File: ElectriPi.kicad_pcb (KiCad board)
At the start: 2 copper layers, 65 x 56 mm, 37 parts, among them J1 2444, J3 JST XH 01x02, J6 Raspberry_Pi_2_3, J8 JST XH 01x02, Q1 30V 4A 44mΩ, Q2 50nA 150V 200mW 200mA, Q3 30V 4A 44mΩ, U1 XL4015

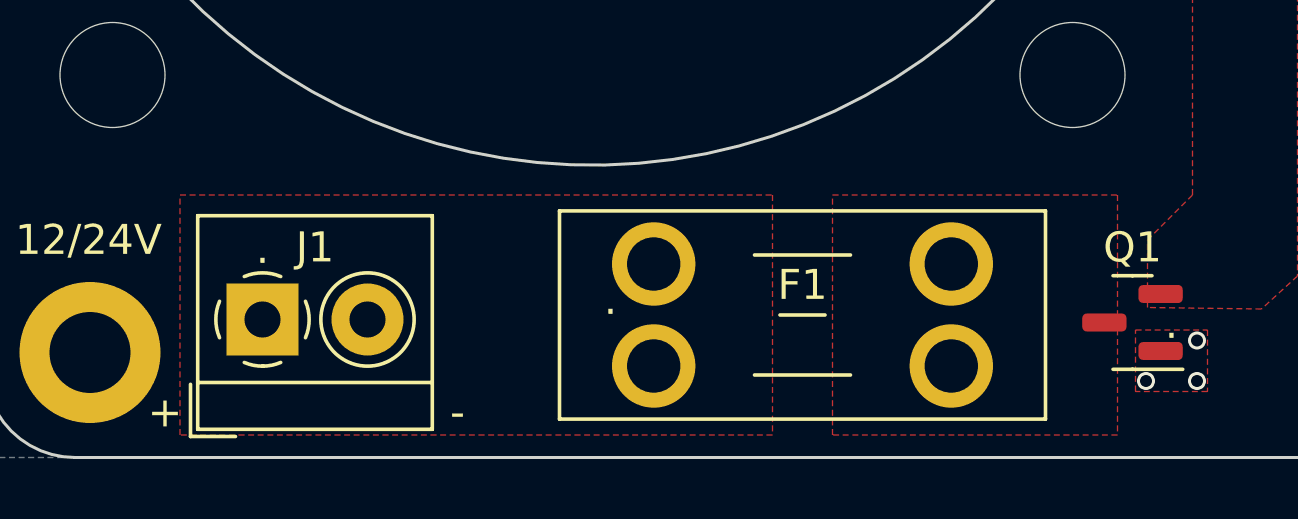
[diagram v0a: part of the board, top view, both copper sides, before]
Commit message: Bladefuse holder switched to Littelfuse nano 2 fuse holder
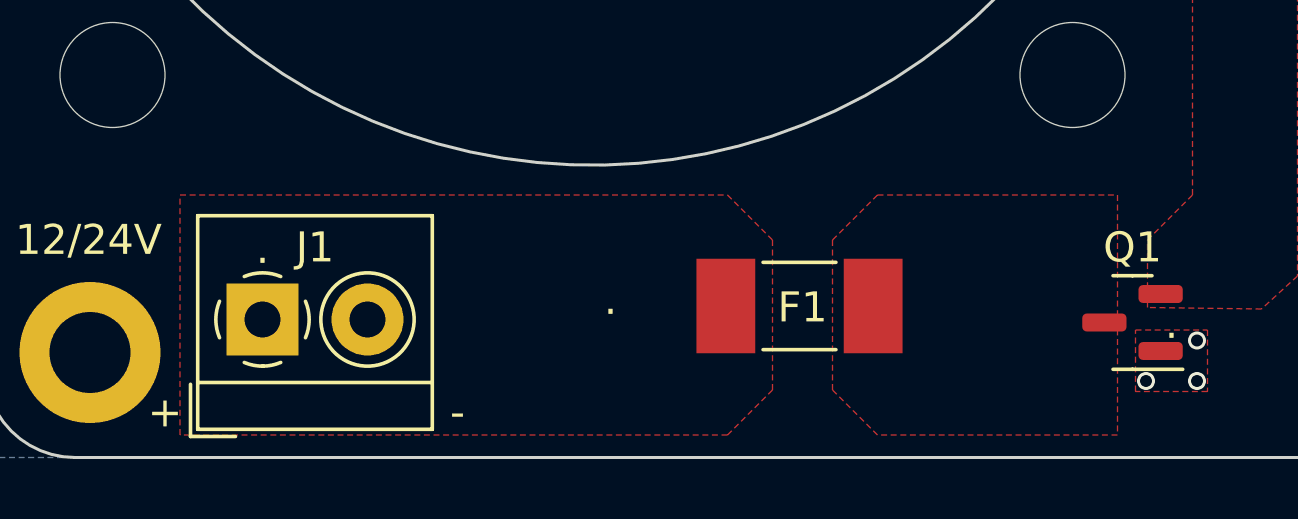
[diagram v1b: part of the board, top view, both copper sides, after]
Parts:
- F1: footprint Fuse:Fuseholder_Blade_Mini_Keystone_3568 -> Fuse:Fuse_Littelfuse-NANO2-451_453
- moved F1 5.06 mm to (112.4, 104.2)

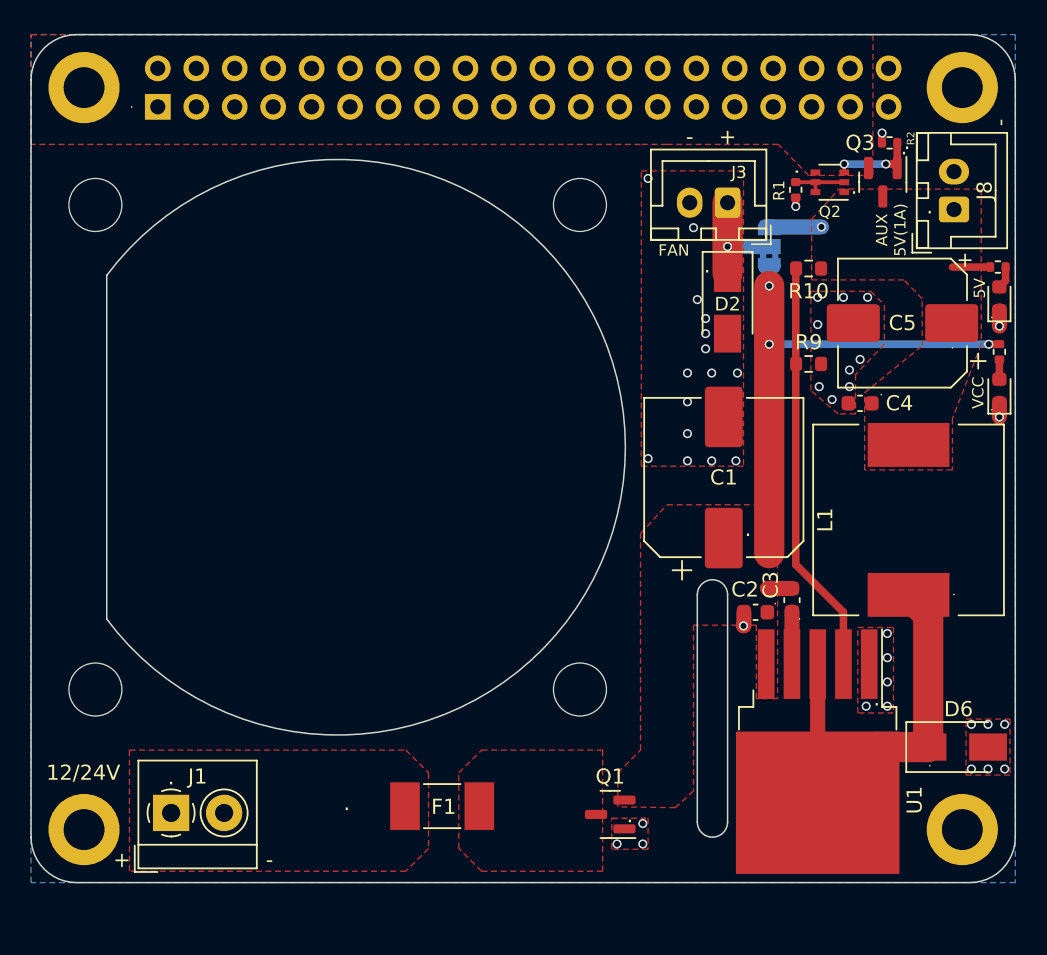
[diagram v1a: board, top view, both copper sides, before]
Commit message: F.Silk, Fan passthough, Fuse, XH input and designator changes
- Added more pin notes to 40Pin GPIO
- Added cutout to fan hole to allow passthrough from reverse mounting
- customised F1 Littelfuse footprint to correctly suit NANO 2 footprint
- Add JST XH Input Option
- Moved superfluous reference designators to hidden layer (user2)
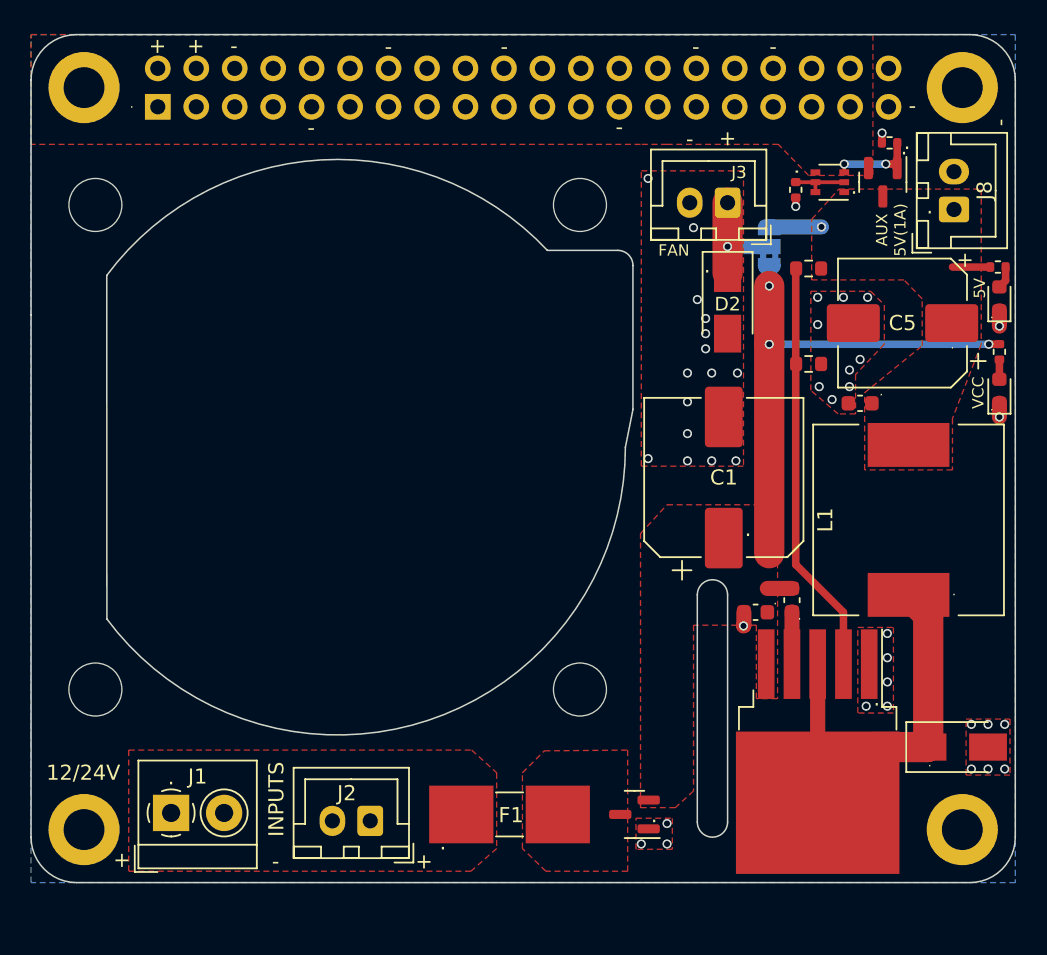
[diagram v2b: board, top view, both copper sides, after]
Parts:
- added J2: JST XH 01x02, Connector_JST:JST_XH_B2B-XH-A_1x02_P2.50mm_Vertical, F.Cu at (107.7, 105.2)
- moved F1 4.48 mm to (116.8, 104.8)
- moved Q1 1.60 mm to (125.1, 104.8)
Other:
- outline, holes or cut-outs redrawn
- board text added: "INPUTS"

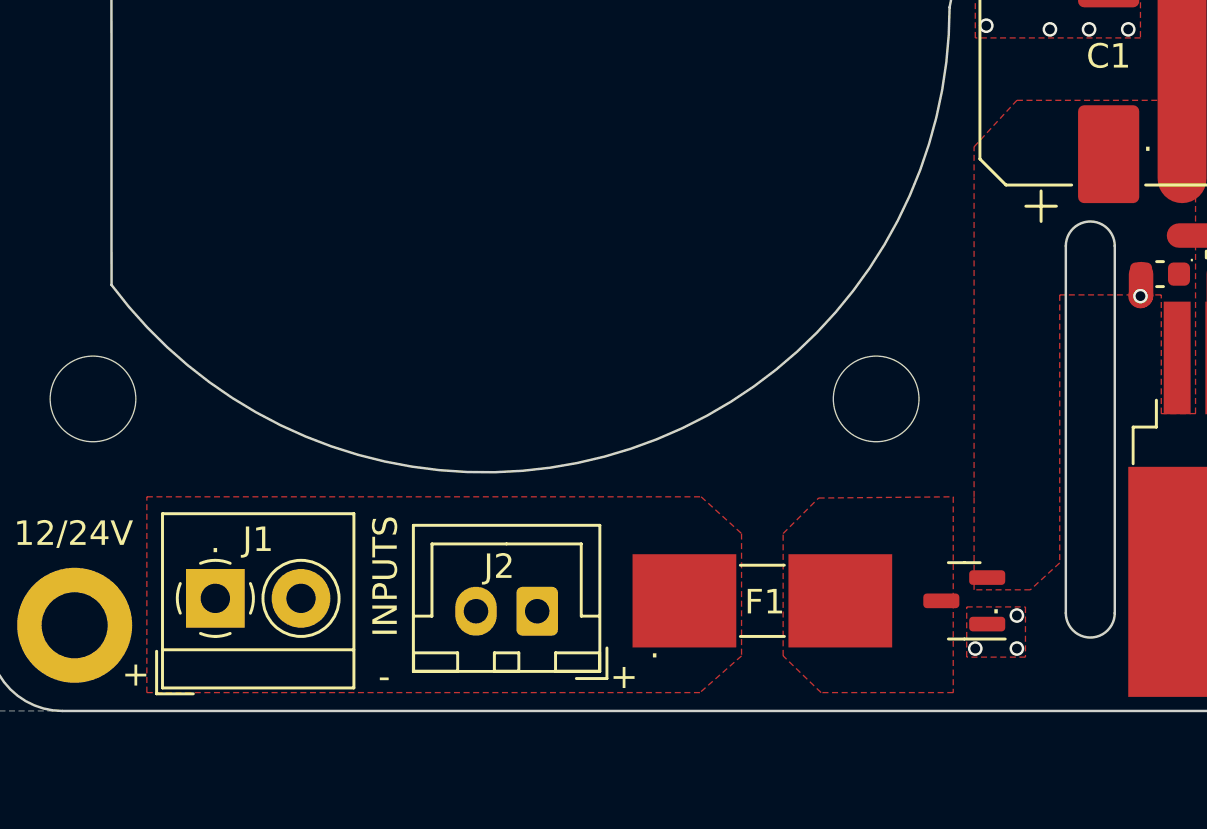
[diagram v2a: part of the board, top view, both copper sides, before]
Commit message: Adding ICL footprint and schematic symbol
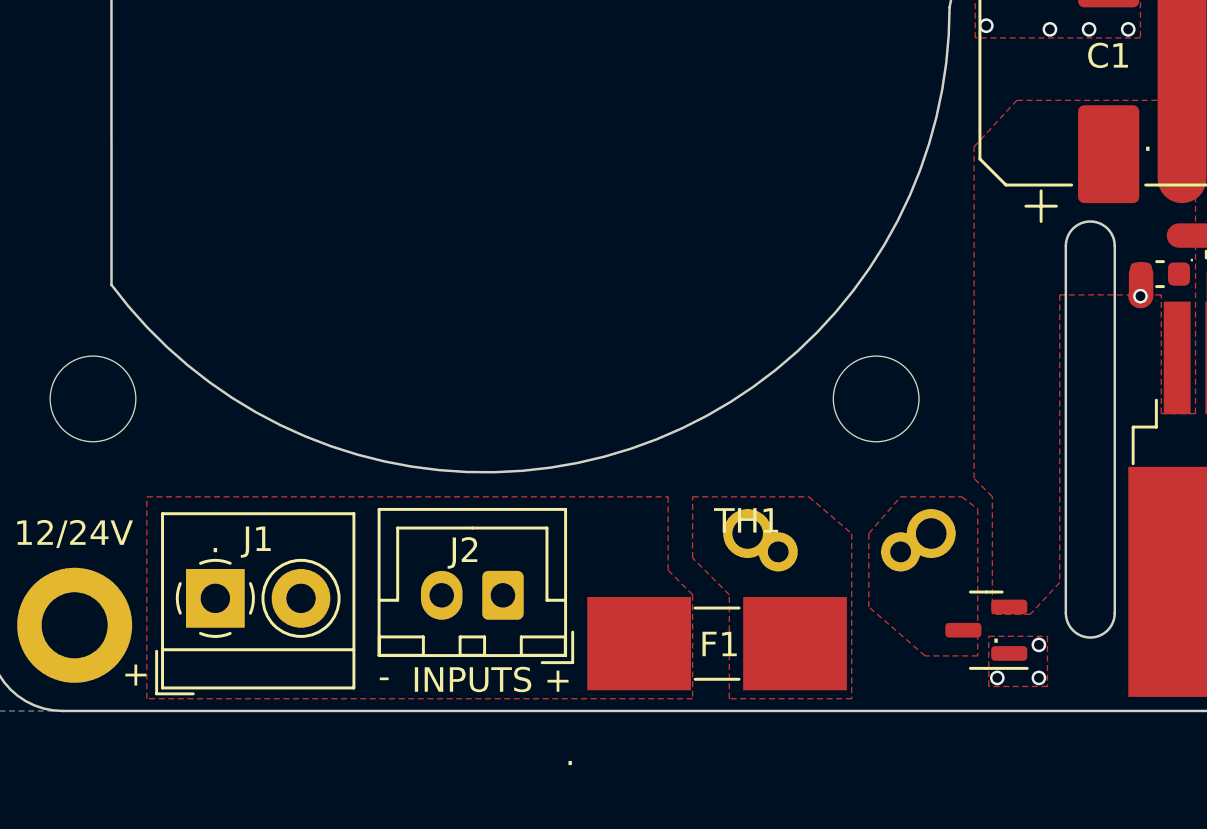
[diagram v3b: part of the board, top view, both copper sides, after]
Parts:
- added TH1: ICL, Inrush_Limiter:5_OR_7pt5_PITCH_ICL, F.Cu at (116.2, 102.0)
- moved F1 2.55 mm to (115.0, 106.5)
- moved J2 1.54 mm to (106.2, 104.5)
- moved Q1 1.50 mm to (126.0, 106.0)
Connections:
- Q1 pad 3: Net-(F1-Pad2) -> Net-(Q1-Pad3)
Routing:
- added copper zone on F.Cu, net Net-(Q1-Pad3)
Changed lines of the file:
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@@
   (net 43 "unconnected-(J6-Pad23)")
   (net 44 "unconnected-(J6-Pad24)")
+  (net 45 "Net-(Q1-Pad3)")
   (footprint "Connector_JST:JST_XH_B2B-XH-A_1x02_P2.50mm_Vertical" (layer "F.Cu")
     (at 146.2 64.8 90)
@@
   )
   (footprint "Connector_JST:JST_XH_B2B-XH-A_1x02_P2.50mm_Vertical" (layer "F.Cu")
-    (at 107.65 105.175 180)
+    (at 106.25 104.525 180)
     (descr "JST XH series connector, B2B-XH-A (http://www.jst-mfg.com/product/pdf/eng/eXH.pdf), generated with kicad-footprint-generator")
     (tags "connector JST XH vertical")
@@
   )
   (footprint "Package_TO_SOT_SMD:SOT-23" (layer "F.Cu")
-    (at 125.1 104.75 180)
+    (at 126 105.95 180)
     (descr "SOT, 3 Pin (https://www.jedec.org/system/files/docs/to-236h.pdf variant AB), generated with kicad-footprint-generator ipc_gullwing_generator.py")
     (tags "SOT TO_SOT_SMD")
@@
       (net 1 "VCC") (pinfunction "S") (pintype "passive"))
     (pad "3" smd roundrect (at 0.9375 0 180) (size 1.475 0.6) (layers "F.Cu" "F.Paste" "F.Mask") (roundrect_rratio 0.25)
-      (net 9 "Net-(F1-Pad2)") (pinfunction "D") (pintype "passive"))
+      (net 45 "Net-(Q1-Pad3)") (pinfunction "D") (pintype "passive"))
     (model "${KICAD6_3DMODEL_DIR}/Package_TO_SOT_SMD.3dshapes/SOT-23.wrl"
       (offset (xyz 0 0 0))
@@
   )
   (footprint "Fuse:Fuse_Littelfuse-NANO2-451_453" (layer "F.Cu")
-    (at 116.85 104.75)
+    (at 115 106.5)
     (descr "Littelfuse NANO2 https://www.littelfuse.com/~/media/electronics/datasheets/fuses/littelfuse_fuse_451_453_datasheet.pdf.pdf")
     (tags "Fuse Nano2")
@@
     )
   )
+  (footprint "Inrush_Limiter:5_OR_7pt5_PITCH_ICL" (layer "F.Cu")
+    (at 116.25 102)
+    (property "Sheetfile" "ElectriPi.kicad_sch")
+    (property "Sheetname" "")
+    (attr through_hole)
+    (fp_text reference "TH1" (at 0 -0.5 unlocked) (layer "F.SilkS")
+      (effects (font (size 1 1) (thickness 0.15)))
+    )
+    (fp_text value "ICL" (at 0 1 unlocked) (layer "F.Fab")
+      (effects (font (size 1 1) (thickness 0.15)))
+    )
+    (pad "1" thru_hole circle (at 1.25 0.75) (size 1.6 1.6) (drill 0.85) (layers *.Cu *.Mask)
+      (net 9 "Net-(F1-Pad2)") (pintype "passive"))
+    (pad "1" thru_hole circle (at 0 0) (size 2 2) (drill 1.25) (layers *.Cu *.Mask)
+      (net 9 "Net-(F1-Pad2)") (pintype "passive"))
+    (pad "2" thru_hole circle (at 7.5 0) (size 2 2) (drill 1.25) (layers *.Cu *.Mask)
+      (net 45 "Net-(Q1-Pad3)") (pintype "passive"))
+    (pad "2" thru_hole circle (at 6.25 0.75) (size 1.6 1.6) (drill 0.85) (layers *.Cu *.Mask)
+      (net 45 "Net-(Q1-Pad3)") (pintype "passive"))
+  )
   (footprint "Resistor_SMD:R_0402_1005Metric" (layer "F.Cu")
     (at 149.2 74.2 90)
@@
     (effects (font (size 1 1) (thickness 0.15)))
   )
-  (gr_text "INPUTS" (at 101.45 103.75 90) (layer "F.SilkS")
+  (gr_text "INPUTS" (at 105 108) (layer "F.SilkS")
     (effects (font (size 1 1) (thickness 0.15)))
   )
-  (gr_text "." (at 126.4 104.8) (layer "F.SilkS")
+  (gr_text "." (at 126.4 106) (layer "F.SilkS")
     (effects (font (size 1 1) (thickness 0.15)))
   )
@@
     (effects (font (size 1 1) (thickness 0.153)))
   )
-  (gr_text "+" (at 111.2 107.85) (layer "F.SilkS")
+  (gr_text "+" (at 108.5 108) (layer "F.SilkS")
     (effects (font (size 1 1) (thickness 0.15)))
   )
@@
     (effects (font (size 1 1) (thickness 0.153)))
   )
-  (gr_text "." (at 112.45 106.6) (layer "F.SilkS")
+  (gr_text "." (at 109 111) (layer "F.SilkS")
     (effects (font (size 1 1) (thickness 0.15)))
   )
@@
   (via (at 149.2 78.5) (size 0.6) (drill 0.4) (layers "F.Cu" "B.Cu") (net 2))
   (via (at 148.45 101.75) (size 0.6) (drill 0.4) (layers "F.Cu" "B.Cu") (free) (net 2))
-  (via (at 125.55 106.7) (size 0.6) (drill 0.4) (layers "F.Cu" "B.Cu") (free) (net 2))
+  (via (at 126.45 107.9) (size 0.6) (drill 0.4) (layers "F.Cu" "B.Cu") (free) (net 2))
   (via (at 140.5 70.6) (size 0.6) (drill 0.4) (layers "F.Cu" "B.Cu") (free) (net 2))
   (via (at 129.8 74) (size 0.6) (drill 0.4) (layers "F.Cu" "B.Cu") (free) (net 2))
@@
   (via (at 128.6 81.4) (size 0.6) (drill 0.4) (layers "F.Cu" "B.Cu") (free) (net 2))
   (via (at 129.25 70.75) (size 0.6) (drill 0.4) (layers "F.Cu" "B.Cu") (free) (net 2))
-  (via (at 127.25 106.7) (size 0.6) (drill 0.4) (layers "F.Cu" "B.Cu") (free) (net 2))
+  (via (at 128.15 107.9) (size 0.6) (drill 0.4) (layers "F.Cu" "B.Cu") (free) (net 2))
   (via (at 137.2 70.6) (size 0.6) (drill 0.4) (layers "F.Cu" "B.Cu") (free) (net 2))
   (via (at 138.15 77.35) (size 0.6) (drill 0.4) (layers "F.Cu" "B.Cu") (free) (net 2))
   (via (at 149.55 98.8) (size 0.6) (drill 0.4) (layers "F.Cu" "B.Cu") (free) (net 2))
   (via (at 147.35 98.8) (size 0.6) (drill 0.4) (layers "F.Cu" "B.Cu") (free) (net 2))
-  (via (at 127.25 105.35) (size 0.6) (drill 0.4) (layers "F.Cu" "B.Cu") (net 2))
+  (via (at 128.15 106.55) (size 0.6) (drill 0.4) (layers "F.Cu" "B.Cu") (net 2))
   (via (at 131.9 75.6) (size 0.6) (drill 0.4) (layers "F.Cu" "B.Cu") (free) (net 2))
   (via (at 141.8 96) (size 0.6) (drill 0.4) (layers "F.Cu" "B.Cu") (free) (net 2))
@@
     (polygon
       (pts
-        (xy 116 107)
-        (xy 114.3 108.5)
-        (xy 91.7 108.5)
+        (xy 114 108.75)
+        (xy 91.7 108.75)
         (xy 91.7 100.5)
-        (xy 114.35 100.5)
-        (xy 116 102)
+        (xy 113 100.5)
+        (xy 113 103.5)
+        (xy 114 104.5)
       )
     )
@@
         (xy 133.15 92.25)
         (xy 129 92.25)
-        (xy 129 103.2)
-        (xy 127.8 104.3)
-        (xy 125.5 104.3)
-        (xy 125.5 100.5)
+        (xy 129 104)
+        (xy 127.8 105.3)
+        (xy 126.25 105.3)
+        (xy 126.25 100.5)
+        (xy 125.5 99.75)
         (xy 125.5 86.2)
         (xy 127.25 84.3)
@@
     )
   )
-  (zone (net 9) (net_name "Net-(F1-Pad2)") (layer "F.Cu") (hatch edge 0.508)
+  (zone (net 45) (net_name "Net-(Q1-Pad3)") (layer "F.Cu") (hatch edge 0.508)
     (connect_pads thru_hole_only (clearance 0.508))
     (min_thickness 0.254) (filled_areas_thickness no)
@@
     (polygon
       (pts
-        (xy 124.65 108.5)
-        (xy 119.25 108.5)
-        (xy 117.7 107)
-        (xy 117.7 102)
-        (xy 119.15 100.55)
-        (xy 124.65 100.5)
+        (xy 125.65 107)
+        (xy 123.5 107)
+        (xy 121.2 105)
+        (xy 121.2 102)
+        (xy 122.5 100.5)
+        (xy 125 100.5)
+        (xy 125.65 101)
       )
     )
@@
     )
   )
+  (zone (net 9) (net_name "Net-(F1-Pad2)") (layer "F.Cu") (hatch edge 0.508)
+    (connect_pads thru_hole_only (clearance 0.508))
+    (min_thickness 0.254) (filled_areas_thickness no)
+    (fill yes (thermal_gap 0.508) (thermal_bridge_width 1.5))
+    (polygon
+      (pts
+        (xy 120.5 102)
+        (xy 120.5 108.75)
+        (xy 115.5 108.75)
+        (xy 115.5 104.5)
+        (xy 114 103)
+        (xy 114 100.5)
+        (xy 118.75 100.5)
+      )
+    )
+  )
   (zone (net 2) (net_name "GND") (layer "F.Cu") (hatch edge 0.508)
     (connect_pads yes (clearance 0.508))
@@
     (polygon
       (pts
-        (xy 127.6 107.05)
-        (xy 125.2 107.05)
-        (xy 125.2 105)
-        (xy 127.6 105)
+        (xy 128.5 108.25)
+        (xy 126.1 108.25)
+        (xy 126.1 106.2)
+        (xy 128.5 106.2)
       )
     )

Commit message: adding test points
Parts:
- added TP1: TestPoint, TestPoint:TestPoint_Pad_D1.5mm, B.Cu at (141.0, 68.5)
- added TP2: TestPoint, TestPoint:TestPoint_Pad_D1.5mm, B.Cu at (110.0, 102.0)
- added TP3: TestPoint, TestPoint:TestPoint_Pad_D1.5mm, B.Cu at (122.5, 105.0)
- added TP4: TestPoint, TestPoint:TestPoint_Pad_D1.5mm, B.Cu at (127.5, 87.5)
- added TP5: TestPoint, TestPoint:TestPoint_Pad_D1.5mm, B.Cu at (136.0, 61.5)
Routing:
- net Net-(Q1-Pad3): track 0.00 -> 4.00 mm, vias 0 -> 1
- net 5V_PI: track 0.00 -> 3.95 mm, vias 0 -> 2
- net VCC: track 35.8 -> 39.3 mm, vias 3 -> 5
- net Net-(F1-Pad1): track 0.00 -> 3.50 mm, vias 0 -> 2
- net +5V: track 5.94 -> 9.44 mm, vias 1 -> 3
